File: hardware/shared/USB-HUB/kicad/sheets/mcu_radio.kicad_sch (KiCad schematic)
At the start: 0 parts

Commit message: feat(hardware): wire 30deg optical ring power and hub USB interfaces for accessibility pointing, ~$9 ring / ~$5-6 hub BOM
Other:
- note added: "MCU/radio interface scaffold: native USB, recovery, and status nets are declared here before component placement."
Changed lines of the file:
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@@
   (generator_version "0.1")
   (paper "A4")
+  (text "MCU/radio interface scaffold: native USB, recovery, and status nets are declared here before component placement."
+    (at 20.32 20.32 0)
+    (effects (font (size 1.27 1.27)))
+  )
+  (hierarchical_label "VREG_3V3"
+    (shape input)
+    (at 25.4 38.1 0)
+    (effects (font (size 1.27 1.27)))
+  )
+  (hierarchical_label "USB_D+"
+    (shape passive)
+    (at 25.4 45.72 0)
+    (effects (font (size 1.27 1.27)))
+  )
+  (hierarchical_label "USB_D-"
+    (shape passive)
+    (at 25.4 53.34 0)
+    (effects (font (size 1.27 1.27)))
+  )
+  (hierarchical_label "EN"
+    (shape input)
+    (at 58.42 109.22 90)
+    (effects (font (size 1.27 1.27)))
+  )
+  (hierarchical_label "BOOT_N"
+    (shape input)
+    (at 66.04 109.22 90)
+    (effects (font (size 1.27 1.27)))
+  )
+  (hierarchical_label "UART_TX_DBG"
+    (shape output)
+    (at 73.66 109.22 90)
+    (effects (font (size 1.27 1.27)))
+  )
+  (hierarchical_label "UART_RX_DBG"
+    (shape input)
+    (at 81.28 109.22 90)
+    (effects (font (size 1.27 1.27)))
+  )
+  (hierarchical_label "LED_STATUS"
+    (shape output)
+    (at 88.9 109.22 90)
+    (effects (font (size 1.27 1.27)))
+  )
   (sheet_instances
     (path "/" (page "1"))

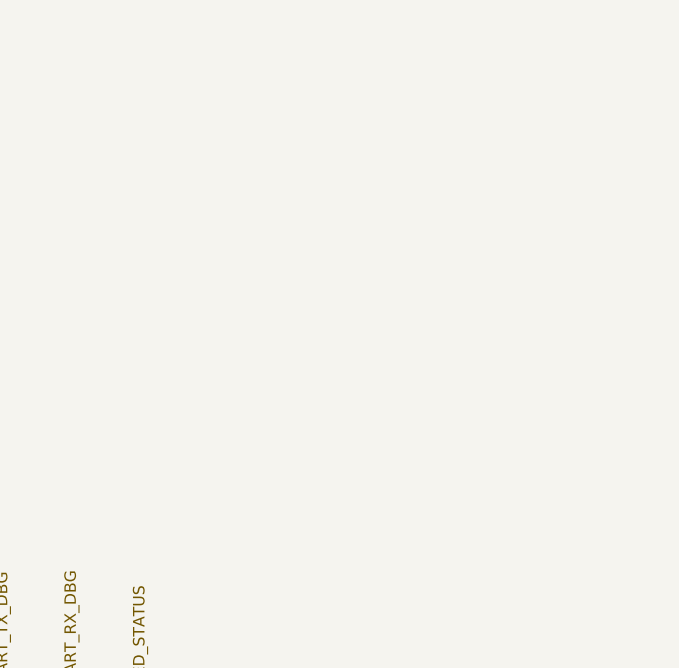
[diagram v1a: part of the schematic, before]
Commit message: feat(usb-hub): add native usb first-board pass
Defensive publication:

- Specific sensing mechanism: no surface sensor on the hub; native USB ESP32-S3 service/programming and HID bridge capture for the PowerFinger BLE input family.

- Form factor and angle: straight inline direct-plug USB-A dongle board, first-pass 54 x 26 mm layout with reinforced SOFNG USB-05 plug retention.

- Intended use case: offline accessible first-board bring-up, repair, programming, and native-USB service for PowerFinger ring/wand development.

- BOM estimate: keeps the active USB-HUB packet inside the current ~$5-6 first-board BOM intent.

Verification:

- git diff --check -- hardware/shared/USB-HUB

- KiCad CLI ERC/DRC run locally and documented as still failing pending schematic connectivity and PCB routing closure.
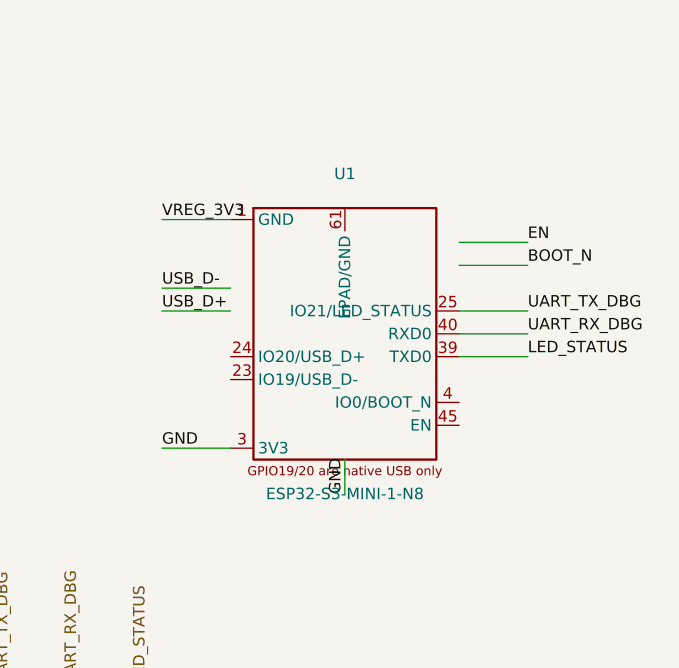
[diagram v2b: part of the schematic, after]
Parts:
- added U1: ESP32-S3-MINI-1-N8, PowerFinger_USB:ESP32-S3-MINI-1-N8_FirstBoard, symbol PowerFinger:ESP32-S3-MINI-1-N8_FirstBoard
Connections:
- net LED_STATUS: now also U1.39 (TXD0)
- net UART_RX_DBG: now also U1.40 (RXD0)
- net UART_TX_DBG: now also U1.25 (IO21/LED_STATUS)
- net VREG_3V3: now also U1.1 (GND)
- new net GND: U1.3 (3V3)
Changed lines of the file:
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@@
     (effects (font (size 1.27 1.27)))
+  )
+  (label "VREG_3V3"
+    (at 91.44 55.88 0)
+    (effects (font (size 1.27 1.27)) (justify left bottom))
+  )
+  (label "USB_D-"
+    (at 91.44 63.5 0)
+    (effects (font (size 1.27 1.27)) (justify left bottom))
+  )
+  (label "USB_D+"
+    (at 91.44 66.04 0)
+    (effects (font (size 1.27 1.27)) (justify left bottom))
+  )
+  (label "GND"
+    (at 91.44 81.28 0)
+    (effects (font (size 1.27 1.27)) (justify left bottom))
+  )
+  (label "EN"
+    (at 132.08 58.42 0)
+    (effects (font (size 1.27 1.27)) (justify left bottom))
+  )
+  (label "BOOT_N"
+    (at 132.08 60.96 0)
+    (effects (font (size 1.27 1.27)) (justify left bottom))
+  )
+  (label "UART_TX_DBG"
+    (at 132.08 66.04 0)
+    (effects (font (size 1.27 1.27)) (justify left bottom))
+  )
+  (label "UART_RX_DBG"
+    (at 132.08 68.58 0)
+    (effects (font (size 1.27 1.27)) (justify left bottom))
+  )
+  (label "LED_STATUS"
+    (at 132.08 71.12 0)
+    (effects (font (size 1.27 1.27)) (justify left bottom))
+  )
+  (label "GND"
+    (at 111.76 86.36 90)
+    (effects (font (size 1.27 1.27)) (justify left bottom))
+  )
+  (wire
+    (pts
+      (xy 91.44 55.88)
+      (xy 99.06 55.88)
+    )
+    (stroke (width 0) (type default) (color 0 0 0 0))
+  )
+  (wire
+    (pts
+      (xy 91.44 63.5)
+      (xy 99.06 63.5)
+    )
+    (stroke (width 0) (type default) (color 0 0 0 0))
+  )
+  (wire
+    (pts
+      (xy 91.44 66.04)
+      (xy 99.06 66.04)
+    )
+    (stroke (width 0) (type default) (color 0 0 0 0))
+  )
+  (wire
+    (pts
+      (xy 91.44 81.28)
+      (xy 99.06 81.28)
+    )
+    (stroke (width 0) (type default) (color 0 0 0 0))
+  )
+  (wire
+    (pts
+      (xy 111.76 82.55)
+      (xy 111.76 86.36)
+    )
+    (stroke (width 0) (type default) (color 0 0 0 0))
+  )
+  (wire
+    (pts
+      (xy 124.46 58.42)
+      (xy 132.08 58.42)
+    )
+    (stroke (width 0) (type default) (color 0 0 0 0))
+  )
+  (wire
+    (pts
+      (xy 124.46 60.96)
+      (xy 132.08 60.96)
+    )
+    (stroke (width 0) (type default) (color 0 0 0 0))
+  )
+  (wire
+    (pts
+      (xy 124.46 66.04)
+      (xy 132.08 66.04)
+    )
+    (stroke (width 0) (type default) (color 0 0 0 0))
+  )
+  (wire
+    (pts
+      (xy 124.46 68.58)
+      (xy 132.08 68.58)
+    )
+    (stroke (width 0) (type default) (color 0 0 0 0))
+  )
+  (wire
+    (pts
+      (xy 124.46 71.12)
+      (xy 132.08 71.12)
+    )
+    (stroke (width 0) (type default) (color 0 0 0 0))
+  )
+  (symbol (lib_id "PowerFinger:ESP32-S3-MINI-1-N8_FirstBoard") (at 111.76 68.58 0) (unit 1)
+    (in_bom yes) (on_board yes) (dnp no) (fields_autoplaced)
+    (property "Reference" "U1" (at 111.76 50.8 0)
+      (effects (font (size 1.27 1.27)))
+    )
+    (property "Value" "ESP32-S3-MINI-1-N8" (at 111.76 86.36 0)
+      (effects (font (size 1.27 1.27)))
+    )
+    (property "Footprint" "PowerFinger_USB:ESP32-S3-MINI-1-N8_FirstBoard" (at 111.76 88.9 0)
+      (effects (font (size 1.27 1.27)) hide)
+    )
+    (property "Datasheet" "https://documentation.espressif.com/esp32-s3-mini-1_mini-1u_datasheet_en.pdf" (at 111.76 91.44 0)
+      (effects (font (size 1.27 1.27)) hide)
+    )
+    (pin "1")
+    (pin "3")
+    (pin "4")
+    (pin "23")
+    (pin "24")
+    (pin "25")
+    (pin "39")
+    (pin "40")
+    (pin "45")
+    (pin "61")
+    (instances
+      (project "usb_hub"
+        (path "/"
+          (reference "U1") (unit 1)
+        )
+      )
+    )
   )
   (sheet_instances

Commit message: feat(usb-hub): clean native USB first board pass
Sensing mechanism: none; native USB-A hub/control accessory capture for the shared USB-HUB packet.

Form factor and angle: direct-plug USB-A dongle first-board PCB; no ring angle applies.

Intended use case: offline native-USB repairable hub/control bring-up for accessibility pointing devices.

BOM estimate: kept inside the current USB-HUB approximately -6 first-board intent.
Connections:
- net BOOT_N: now also U1.4 (IO0/BOOT_N)
- net EN: now also U1.45 (EN)
- net GND: now also U1.1 (GND), U1.61 (EPAD/GND); no longer U1.3 (3V3)
- net USB_D+: now also U1.24 (IO20/USB_D+)
- net USB_D-: now also U1.23 (IO19/USB_D-)
- net VREG_3V3: now also U1.3 (3V3); no longer U1.1 (GND)
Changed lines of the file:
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@@
   )
   (label "VREG_3V3"
+    (at 38.1 38.1 0)
+    (effects (font (size 1.27 1.27)) (justify left bottom))
+  )
+  (label "USB_D+"
+    (at 38.1 45.72 0)
+    (effects (font (size 1.27 1.27)) (justify left bottom))
+  )
+  (label "USB_D-"
+    (at 38.1 53.34 0)
+    (effects (font (size 1.27 1.27)) (justify left bottom))
+  )
+  (label "EN"
+    (at 58.42 101.6 90)
+    (effects (font (size 1.27 1.27)) (justify left bottom))
+  )
+  (label "BOOT_N"
+    (at 66.04 101.6 90)
+    (effects (font (size 1.27 1.27)) (justify left bottom))
+  )
+  (label "UART_TX_DBG"
+    (at 73.66 101.6 90)
+    (effects (font (size 1.27 1.27)) (justify left bottom))
+  )
+  (label "UART_RX_DBG"
+    (at 81.28 101.6 90)
+    (effects (font (size 1.27 1.27)) (justify left bottom))
+  )
+  (label "LED_STATUS"
+    (at 88.9 101.6 90)
+    (effects (font (size 1.27 1.27)) (justify left bottom))
+  )
+  (label "GND"
     (at 91.44 55.88 0)
     (effects (font (size 1.27 1.27)) (justify left bottom))
   )
+  (label "USB_D+"
+    (at 91.44 71.12 0)
+    (effects (font (size 1.27 1.27)) (justify left bottom))
+  )
   (label "USB_D-"
-    (at 91.44 63.5 0)
+    (at 91.44 73.66 0)
+    (effects (font (size 1.27 1.27)) (justify left bottom))
+  )
+  (label "VREG_3V3"
+    (at 91.44 81.28 0)
     (effects (font (size 1.27 1.27)) (justify left bottom))
   )
   (label "USB_D+"
-    (at 91.44 66.04 0)
+    (at 91.44 71.12 0)
     (effects (font (size 1.27 1.27)) (justify left bottom))
   )
   (label "GND"
-    (at 91.44 81.28 0)
+    (at 111.76 50.8 90)
     (effects (font (size 1.27 1.27)) (justify left bottom))
   )
   (label "EN"
-    (at 132.08 58.42 0)
+    (at 132.08 78.74 0)
     (effects (font (size 1.27 1.27)) (justify left bottom))
   )
   (label "BOOT_N"
-    (at 132.08 60.96 0)
+    (at 132.08 76.2 0)
     (effects (font (size 1.27 1.27)) (justify left bottom))
   )
@@
     (effects (font (size 1.27 1.27)) (justify left bottom))
   )
-  (label "GND"
-    (at 111.76 86.36 90)
-    (effects (font (size 1.27 1.27)) (justify left bottom))
+  (wire
+    (pts
+      (xy 25.4 38.1)
+      (xy 38.1 38.1)
+    )
+    (stroke (width 0) (type default) (color 0 0 0 0))
+  )
+  (wire
+    (pts
+      (xy 25.4 45.72)
+      (xy 38.1 45.72)
+    )
+    (stroke (width 0) (type default) (color 0 0 0 0))
+  )
+  (wire
+    (pts
+      (xy 25.4 53.34)
+      (xy 38.1 53.34)
+    )
+    (stroke (width 0) (type default) (color 0 0 0 0))
+  )
+  (wire
+    (pts
+      (xy 58.42 109.22)
+      (xy 58.42 101.6)
+    )
+    (stroke (width 0) (type default) (color 0 0 0 0))
+  )
+  (wire
+    (pts
+      (xy 66.04 109.22)
+      (xy 66.04 101.6)
+    )
+    (stroke (width 0) (type default) (color 0 0 0 0))
+  )
+  (wire
+    (pts
+      (xy 73.66 109.22)
+      (xy 73.66 101.6)
+    )
+    (stroke (width 0) (type default) (color 0 0 0 0))
+  )
+  (wire
+    (pts
+      (xy 81.28 109.22)
+      (xy 81.28 101.6)
+    )
+    (stroke (width 0) (type default) (color 0 0 0 0))
+  )
+  (wire
+    (pts
+      (xy 88.9 109.22)
+      (xy 88.9 101.6)
+    )
+    (stroke (width 0) (type default) (color 0 0 0 0))
   )
   (wire
@@
   (wire
     (pts
-      (xy 91.44 63.5)
-      (xy 99.06 63.5)
-    )
-    (stroke (width 0) (type default) (color 0 0 0 0))
-  )
-  (wire
-    (pts
-      (xy 91.44 66.04)
-      (xy 99.06 66.04)
+      (xy 91.44 71.12)
+      (xy 99.06 71.12)
+    )
+    (stroke (width 0) (type default) (color 0 0 0 0))
+  )
+  (wire
+    (pts
+      (xy 91.44 73.66)
+      (xy 99.06 73.66)
     )
     (stroke (width 0) (type default) (color 0 0 0 0))
@@
   (wire
     (pts
-      (xy 111.76 82.55)
-      (xy 111.76 86.36)
-    )
-    (stroke (width 0) (type default) (color 0 0 0 0))
-  )
-  (wire
-    (pts
-      (xy 124.46 58.42)
-      (xy 132.08 58.42)
-    )
-    (stroke (width 0) (type default) (color 0 0 0 0))
-  )
-  (wire
-    (pts
-      (xy 124.46 60.96)
-      (xy 132.08 60.96)
+      (xy 111.76 54.61)
+      (xy 111.76 50.8)
     )
     (stroke (width 0) (type default) (color 0 0 0 0))
@@
     (stroke (width 0) (type default) (color 0 0 0 0))
   )
+  (wire
+    (pts
+      (xy 124.46 76.2)
+      (xy 132.08 76.2)
+    )
+    (stroke (width 0) (type default) (color 0 0 0 0))
+  )
+  (wire
+    (pts
+      (xy 124.46 78.74)
+      (xy 132.08 78.74)
+    )
+    (stroke (width 0) (type default) (color 0 0 0 0))
+  )
+  (symbol (lib_id "power:PWR_FLAG") (at 91.44 55.88 0) (unit 1)
+    (in_bom no) (on_board no) (dnp no)
+    (property "Reference" "#FLG0301" (at 91.44 53.975 0)
+      (effects (font (size 1.27 1.27)) hide)
+    )
+    (property "Value" "PWR_FLAG" (at 91.44 52.07 0)
+      (effects (font (size 1.27 1.27)))
+    )
+    (pin "1")
+    (instances
+      (project "usb_hub"
+        (path "/"
+          (reference "#FLG0301") (unit 1)
+        )
+      )
+    )
+  )
   (symbol (lib_id "PowerFinger:ESP32-S3-MINI-1-N8_FirstBoard") (at 111.76 68.58 0) (unit 1)

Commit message: fix(usb-hub): clean native-usb dongle drc parity
Direct-plug native USB hub dongle for accessibility pointing and OCR composition; no sensing mechanism change; BOM intent remains ~-6.
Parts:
- added C1A: 100nF, Capacitor_SMD:C_0402_1005Metric, symbol PowerFinger:C_0402_SUPPORT
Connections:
- net GND: now also U1.2 (GND), U1.42 (GND), U1.43 (GND), U1.46 (GND), U1.47 (GND), U1.48 (GND), U1.49 (GND), U1.50 (GND), U1.51 (GND), U1.52 (GND), U1.53 (GND), U1.54 (GND), U1.55 (GND), U1.56 (GND), U1.57 (GND), U1.58 (GND), U1.59 (GND), U1.60 (GND), U1.62 (GND), U1.63 (GND), U1.64 (GND), U1.65 (GND), C1A.2
- net LED_STATUS: now also U1.25 (IO21/LED_STATUS); no longer U1.39 (TXD0)
- net UART_TX_DBG: now also U1.39 (TXD0); no longer U1.25 (IO21/LED_STATUS)
- net VREG_3V3: now also C1A.1
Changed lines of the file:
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@@
     (effects (font (size 1.27 1.27)) (justify left bottom))
   )
-  (label "GND"
+  (hierarchical_label "GND"
+    (shape passive)
     (at 91.44 55.88 0)
     (effects (font (size 1.27 1.27)) (justify left bottom))
@@
     (effects (font (size 1.27 1.27)) (justify left bottom))
   )
-  (label "UART_TX_DBG"
+  (label "LED_STATUS"
     (at 132.08 66.04 0)
     (effects (font (size 1.27 1.27)) (justify left bottom))
@@
     (effects (font (size 1.27 1.27)) (justify left bottom))
   )
-  (label "LED_STATUS"
+  (label "UART_TX_DBG"
     (at 132.08 71.12 0)
     (effects (font (size 1.27 1.27)) (justify left bottom))
@@
     )
     (stroke (width 0) (type default) (color 0 0 0 0))
+  )
+  (label "VREG_3V3"
+    (at 50.8 68.58 0)
+    (effects (font (size 1.27 1.27)) (justify left bottom))
+  )
+  (label "GND"
+    (at 66.04 68.58 0)
+    (effects (font (size 1.27 1.27)) (justify left bottom))
+  )
+  (wire
+    (pts
+      (xy 50.8 68.58)
+      (xy 55.88 68.58)
+    )
+    (stroke (width 0) (type default) (color 0 0 0 0))
+  )
+  (wire
+    (pts
+      (xy 60.96 68.58)
+      (xy 66.04 68.58)
+    )
+    (stroke (width 0) (type default) (color 0 0 0 0))
+  )
+  (symbol (lib_id "PowerFinger:C_0402_SUPPORT") (at 58.42 68.58 0) (unit 1)
+    (in_bom yes) (on_board yes) (dnp no) (fields_autoplaced)
+    (property "Reference" "C1A" (at 53.34 62.23 0)
+      (effects (font (size 1.27 1.27)) (justify left))
+    )
+    (property "Value" "100nF" (at 53.34 64.77 0)
+      (effects (font (size 1.27 1.27)) (justify left))
+    )
+    (property "Footprint" "Capacitor_SMD:C_0402_1005Metric" (at 58.42 58.42 0)
+      (effects (font (size 1.27 1.27)) hide)
+    )
+    (property "Datasheet" "" (at 58.42 55.88 0)
+      (effects (font (size 1.27 1.27)) hide)
+    )
+    (pin "1")
+    (pin "2")
+    (instances
+      (project "usb_hub"
+        (path "/"
+          (reference "C1A") (unit 1)
+        )
+      )
+    )
   )
   (symbol (lib_id "power:PWR_FLAG") (at 91.44 55.88 0) (unit 1)
@@
     )
     (pin "1")
+    (pin "2")
     (pin "3")
     (pin "4")
@@
     (pin "39")
     (pin "40")
+    (pin "42")
+    (pin "43")
     (pin "45")
+    (pin "46")
+    (pin "47")
+    (pin "48")
+    (pin "49")
+    (pin "50")
+    (pin "51")
+    (pin "52")
+    (pin "53")
+    (pin "54")
+    (pin "55")
+    (pin "56")
+    (pin "57")
+    (pin "58")
+    (pin "59")
+    (pin "60")
     (pin "61")
+    (pin "62")
+    (pin "63")
+    (pin "64")
+    (pin "65")
     (instances
       (project "usb_hub"

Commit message: fix(usb-hub): pin local first-board footprints
Design disclosure: sensing mechanism none; form factor stepped USB-A direct-plug USB-HUB dongle; intended use offline BLE HID composition and service access for accessibility; BOM estimate ~$5-6 packet target.

Move first-board commodity/support footprints into the source-controlled PowerFinger_USB library and update the packet verification story to all-severity PCB DRC clean.
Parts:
- C1A: footprint Capacitor_SMD:C_0402_1005Metric -> PowerFinger_USB:C_0402_1005Metric_FirstBoard
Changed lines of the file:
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@@
       (effects (font (size 1.27 1.27)) (justify left))
     )
-    (property "Footprint" "Capacitor_SMD:C_0402_1005Metric" (at 58.42 58.42 0)
+    (property "Footprint" "PowerFinger_USB:C_0402_1005Metric_FirstBoard" (at 58.42 58.42 0)
       (effects (font (size 1.27 1.27)) hide)
     )

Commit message: fix(usb-hub): close kicad erc snapshot
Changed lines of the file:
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@@
-    )
-  )
-  (symbol (lib_id "power:PWR_FLAG") (at 91.44 55.88 0) (unit 1)
-    (in_bom no) (on_board no) (dnp no)
-    (property "Reference" "#FLG0301" (at 91.44 53.975 0)
-      (effects (font (size 1.27 1.27)) hide)
-    )
-    (property "Value" "PWR_FLAG" (at 91.44 52.07 0)
-      (effects (font (size 1.27 1.27)))
-    )
-    (pin "1")
-    (instances
-      (project "usb_hub"
-        (path "/"
-          (reference "#FLG0301") (unit 1)
-        )
-      )
     )
   )
